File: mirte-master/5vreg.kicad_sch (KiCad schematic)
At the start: 1 part, among them J21 5v_regulator

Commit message: mirte master parts jclpcb fixed
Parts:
- removed J21: 5v_regulator, TerminalBlock_Phoenix:TerminalBlock_Phoenix_PT-1,5-4-5.0-H_1x04_P5.00mm_Horizontal, symbol Connector:Screw_Terminal_01x04
- added J23 (x2): sc, easyeda:CONN-TH_XY126V-5.0-2P, symbol Connector:Screw_Terminal_01x02
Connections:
- net +12V: now also J23.1 (Pin_1)
- net +5V: now also J23.2 (Pin_2)
- net GND: now also J23.1 (Pin_1), J23.2 (Pin_2)
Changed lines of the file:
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@@
     (stroke (width 0) (type default))
+  )
+  (symbol (lib_id "Connector:Screw_Terminal_01x02") (at 124.46 90.17 0) (mirror x) (unit 1)
+    (in_bom yes) (on_board yes) (dnp no)
+    (property "Reference" "J23" (at 127 90.17 0)
+      (effects (font (size 1.27 1.27)) (justify left))
+    )
+    (property "Value" "sc" (at 127 87.63 0)
+      (effects (font (size 1.27 1.27)) (justify left))
+    )
+    (property "Footprint" "easyeda:CONN-TH_XY126V-5.0-2P" (at 124.46 90.17 0)
+      (effects (font (size 1.27 1.27)) hide)
+    )
+    (property "Datasheet" "~" (at 124.46 90.17 0)
+      (effects (font (size 1.27 1.27)) hide)
+    )
+    (property "LCSC" "C557646" (at 124.46 90.17 0)
+      (effects (font (size 1.27 1.27)) hide)
+    )
+    (pin "2")
+    (pin "1")
+    (instances
+      (project "mirte-master"
+        (path "/19794465-0368-488c-958e-83b02754ebd6/17ebe4c8-09bb-4699-976c-396d27e4a3f5/cd5c3f96-e789-467d-9a0a-1e1e5a42c039"
+          (reference "J23") (unit 1)
+        )
+        (path "/19794465-0368-488c-958e-83b02754ebd6/17ebe4c8-09bb-4699-976c-396d27e4a3f5/1f6ba3bd-b93c-4e80-aba0-1409dab869f7"
+          (reference "J13") (unit 1)
+        )
+      )
+    )
   )
   (symbol (lib_id "power:GND") (at 113.03 78.74 0) (unit 1)
@@
     )
   )
-  (symbol (lib_id "Connector:Screw_Terminal_01x04") (at 124.46 87.63 0) (mirror x) (unit 1)
-    (in_bom yes) (on_board yes) (dnp no)
-    (property "Reference" "J21" (at 127 87.63 0)
+  (symbol (lib_id "Connector:Screw_Terminal_01x02") (at 124.46 82.55 0) (unit 1)
+    (in_bom yes) (on_board yes) (dnp no) (fields_autoplaced)
+    (property "Reference" "J23" (at 127 82.55 0)
       (effects (font (size 1.27 1.27)) (justify left))
     )
-    (property "Value" "5v_regulator" (at 127 85.09 0)
+    (property "Value" "sc" (at 127 85.09 0)
       (effects (font (size 1.27 1.27)) (justify left))
     )
-    (property "Footprint" "TerminalBlock_Phoenix:TerminalBlock_Phoenix_PT-1,5-4-5.0-H_1x04_P5.00mm_Horizontal" (at 124.46 87.63 0)
+    (property "Footprint" "easyeda:CONN-TH_XY126V-5.0-2P" (at 124.46 82.55 0)
       (effects (font (size 1.27 1.27)) hide)
     )
-    (property "Datasheet" "~" (at 124.46 87.63 0)
+    (property "Datasheet" "~" (at 124.46 82.55 0)
       (effects (font (size 1.27 1.27)) hide)
     )
-    (property "LCSC" "C3034542" (at 127 87.63 0)
+    (property "LCSC" "C557646" (at 124.46 82.55 0)
       (effects (font (size 1.27 1.27)) hide)
     )
+    (pin "2")
     (pin "1")
-    (pin "4")
-    (pin "3")
-    (pin "2")
     (instances
       (project "mirte-master"
+        (path "/19794465-0368-488c-958e-83b02754ebd6/17ebe4c8-09bb-4699-976c-396d27e4a3f5/cd5c3f96-e789-467d-9a0a-1e1e5a42c039"
+          (reference "J23") (unit 1)
+        )
         (path "/19794465-0368-488c-958e-83b02754ebd6/17ebe4c8-09bb-4699-976c-396d27e4a3f5/1f6ba3bd-b93c-4e80-aba0-1409dab869f7"
-          (reference "J21") (unit 1)
+          (reference "J14") (unit 1)
         )
       )

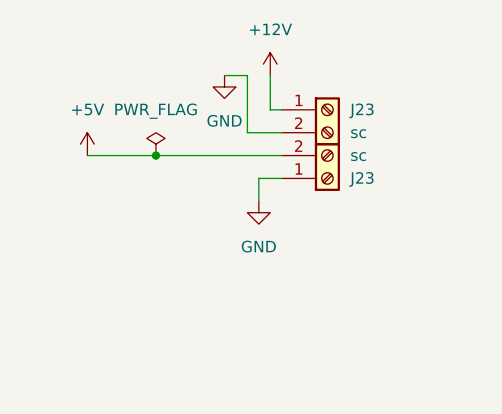
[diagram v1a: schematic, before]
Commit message: mirte-master schematic cleanup and readabilityimprovements
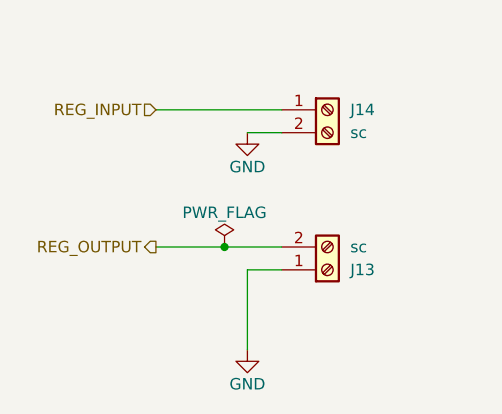
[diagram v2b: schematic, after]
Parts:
- renumbered J23 to J13, J23 to J14
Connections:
- net +12V renamed REG_INPUT
- net +5V renamed REG_OUTPUT
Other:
- title: (none) -> ${PROJECTNAME}
- moved on the sheet: J13
